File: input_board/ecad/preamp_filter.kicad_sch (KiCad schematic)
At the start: 55 parts, among them U2 MC33079, U3 MC33079

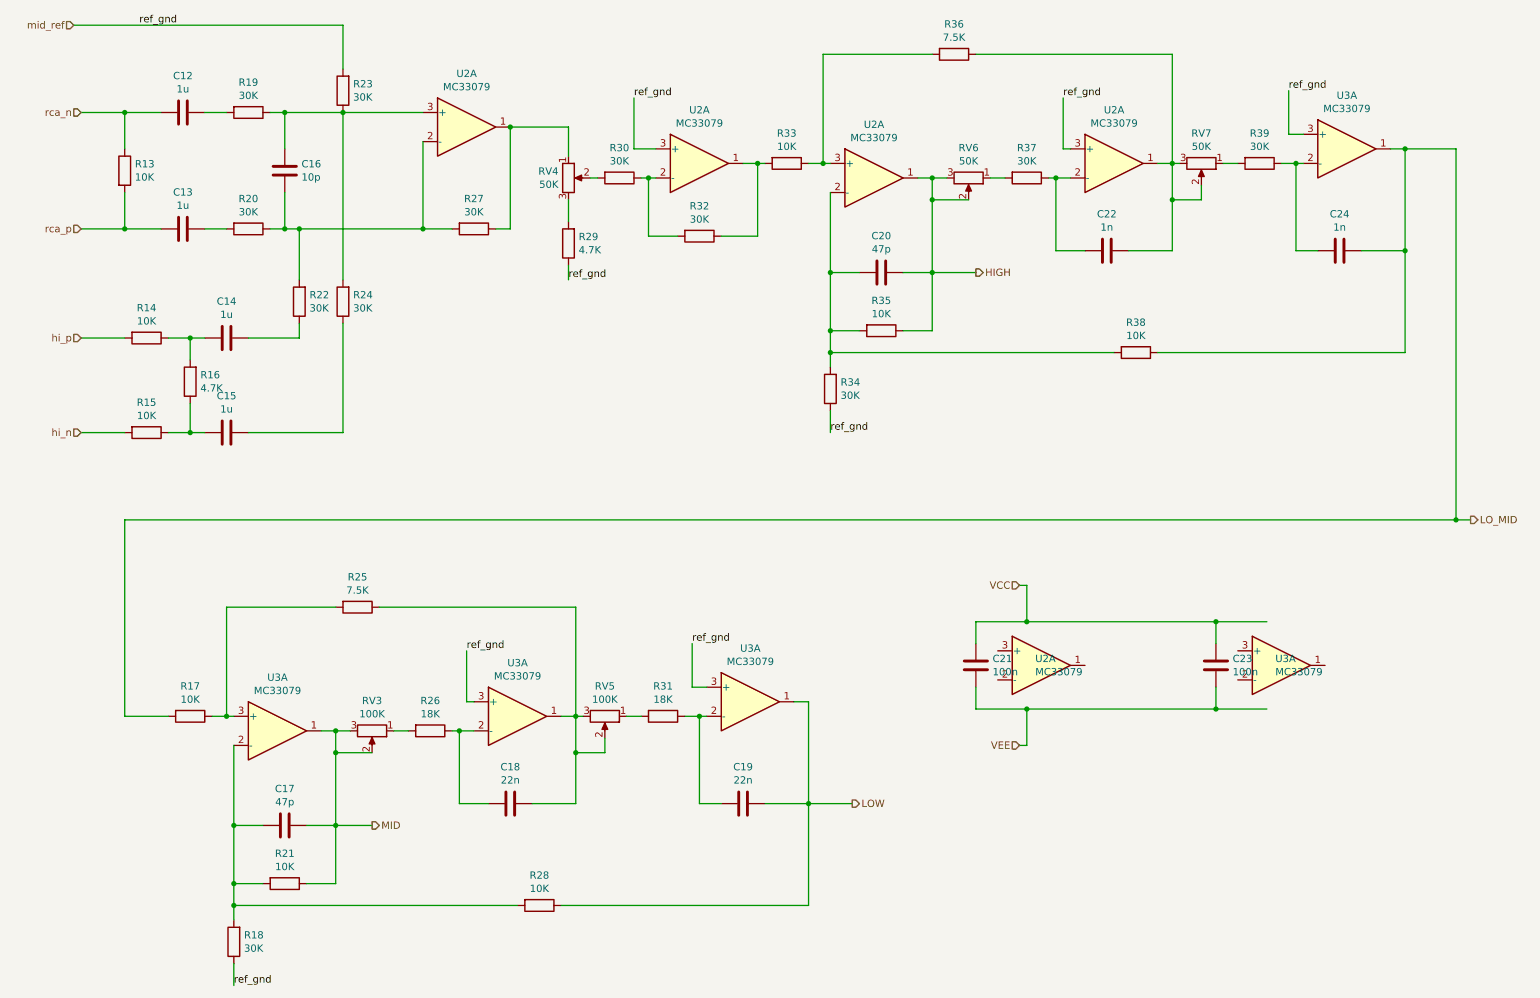
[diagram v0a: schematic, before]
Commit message: Input board: fix scematic and initial version of layout
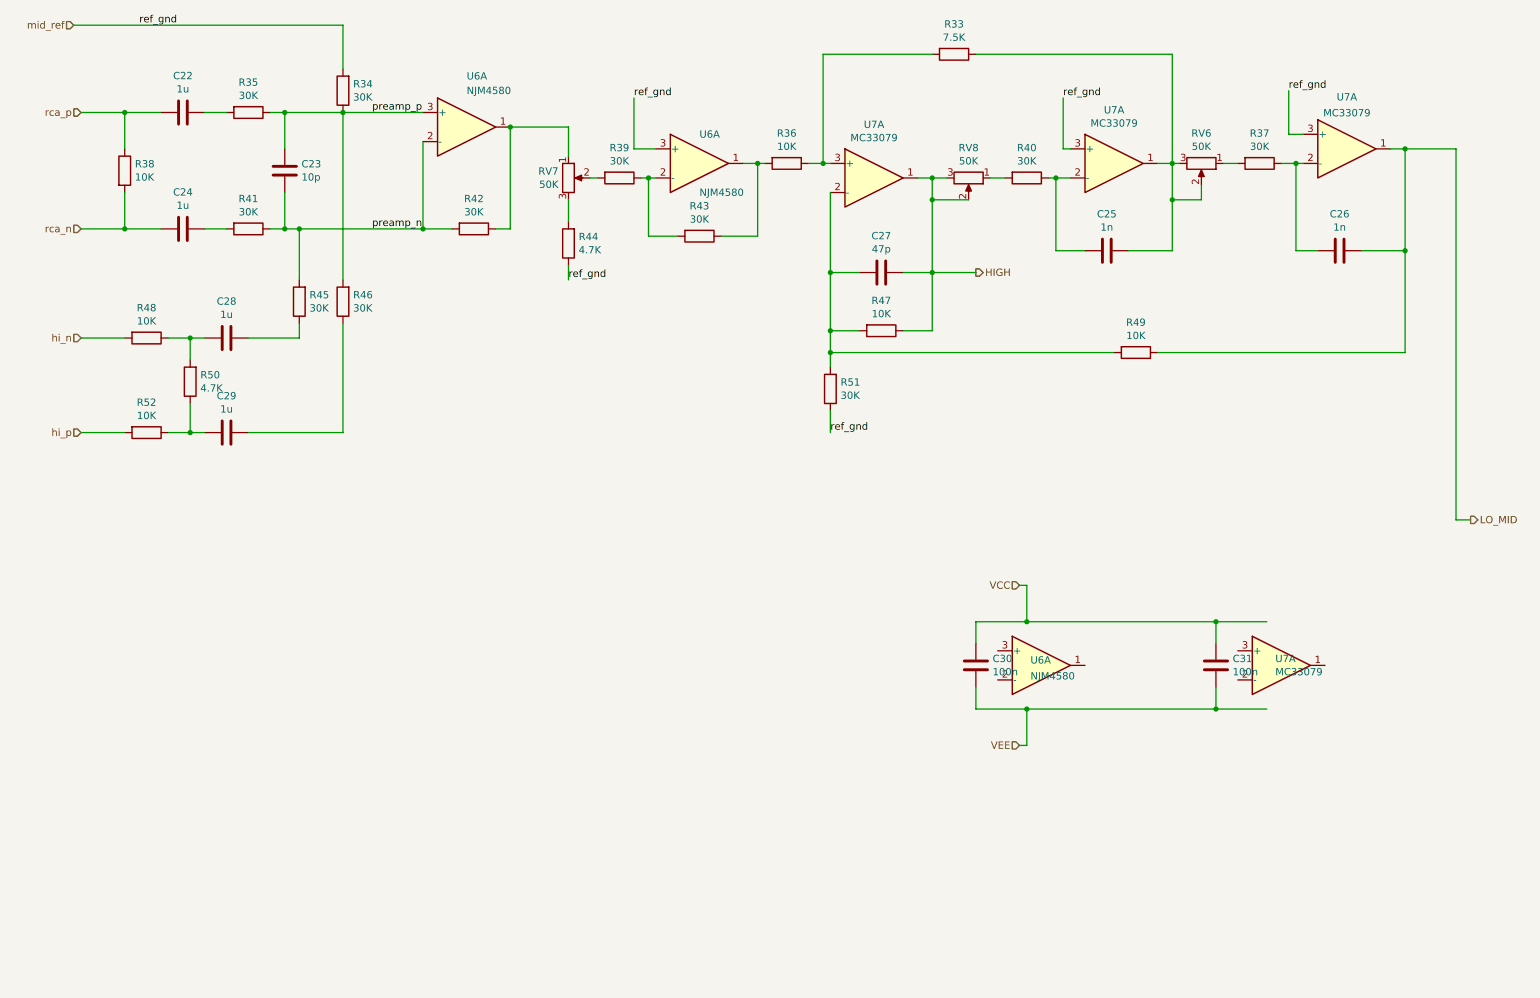
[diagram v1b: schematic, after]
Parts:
- removed C17: 47p, Capacitor_THT:C_Disc_D5.0mm_W2.5mm_P5.00mm, symbol Device:C
- removed C18, C19: 22n, Capacitor_THT:C_Rect_L7.2mm_W2.5mm_P5.00mm_FKS2_FKP2_MKS2_MKP2, symbol Device:C
- removed R17, R21, R28: 10K, Resistor_SMD:R_0805_2012Metric_Pad1.20x1.40mm_HandSolder, symbol Device:R
- removed R18: 30K, Resistor_SMD:R_0805_2012Metric_Pad1.20x1.40mm_HandSolder, symbol Device:R
- removed R25: 7.5K, Resistor_SMD:R_0805_2012Metric_Pad1.20x1.40mm_HandSolder, symbol Device:R
- removed R26, R31: 18K, Resistor_SMD:R_0805_2012Metric_Pad1.20x1.40mm_HandSolder, symbol Device:R
- removed RV3, RV5: 100K, Potentiometer_THT:Potentiometer_Runtron_RM-063_Horizontal, symbol Device:R_POT
- removed U2, U3 (x4): MC33079, Package_SO:SOIC-14_3.9x8.7mm_P1.27mm, symbol Amplifier_Operational:MC33079
- added U6: NJM4580, Package_SO:SOIC-8_3.9x4.9mm_P1.27mm, symbol Amplifier_Operational:NJM4580
- added U7: MC33079, symbol Amplifier_Operational:MC33079
- U6: renamed from U2; value MC33079 -> NJM4580; footprint Package_SO:SOIC-14_3.9x8.7mm_P1.27mm -> Package_SO:SOIC-8_3.9x4.9mm_P1.27mm; symbol Amplifier_Operational:MC33079 -> Amplifier_Operational:NJM4580
- U7: renamed from U2; footprint Package_SO:SOIC-14_3.9x8.7mm_P1.27mm -> (none)
- U7: renamed from U3; footprint Package_SO:SOIC-14_3.9x8.7mm_P1.27mm -> (none)
- renumbered C12 to C22, C16 to C23, C13 to C24, C22 to C25, C24 to C26, C20 to C27, C14 to C28, C15 to C29, C21 to C30, C23 to C31, R36 to R33, R23 to R34, R19 to R35, R33 to R36, R39 to R37, R13 to R38, R30 to R39, R37 to R40, R20 to R41, R27 to R42, R32 to R43, R29 to R44, R22 to R45, R24 to R46, R35 to R47, R14 to R48, R38 to R49, R16 to R50, R34 to R51, R15 to R52, RV7 to RV6, RV4 to RV7, RV6 to RV8
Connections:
- net LO_MID: now also U7.1
- net hi_n: now also R48.2; no longer R52.2
- net hi_p: now also R52.2; no longer R48.2
- net mid_ref: now also U7.3 (+)
- net rca_n: now also C24.2, R38.2; no longer C22.2, R38.1
- net rca_p: now also C22.2, R38.1; no longer C24.2, R38.2
- net preamp_p: now reaches C23.2, R34.1, R35.1, R46.2, U6.3 (+)
- net preamp_n: now reaches C23.1, R41.1, R42.2, R45.2, U6.2 (-)
- net at C26.2, R37.1: now also U7.2 (-)
